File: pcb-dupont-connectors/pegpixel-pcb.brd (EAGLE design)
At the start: 21.6 x 14.2 mm, 5 parts

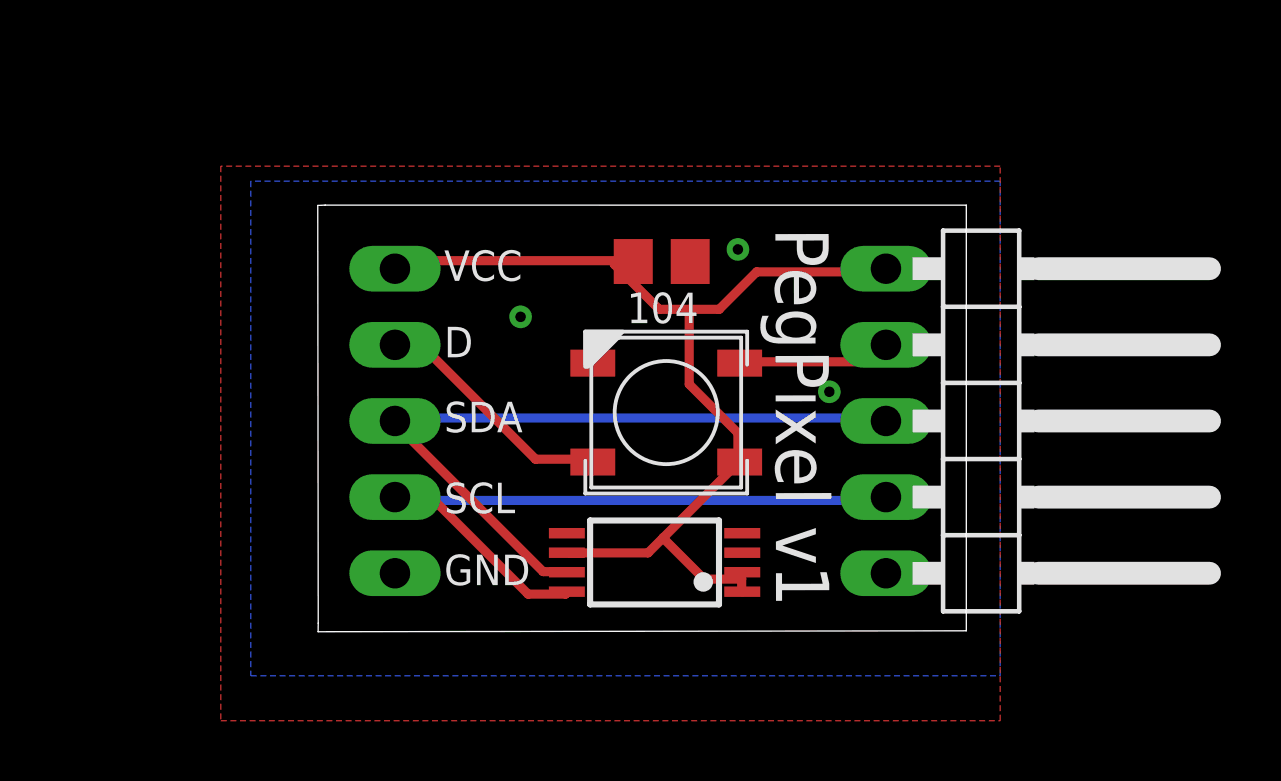
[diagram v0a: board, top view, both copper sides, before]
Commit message: mirror and turn input pin header to place it on top layer
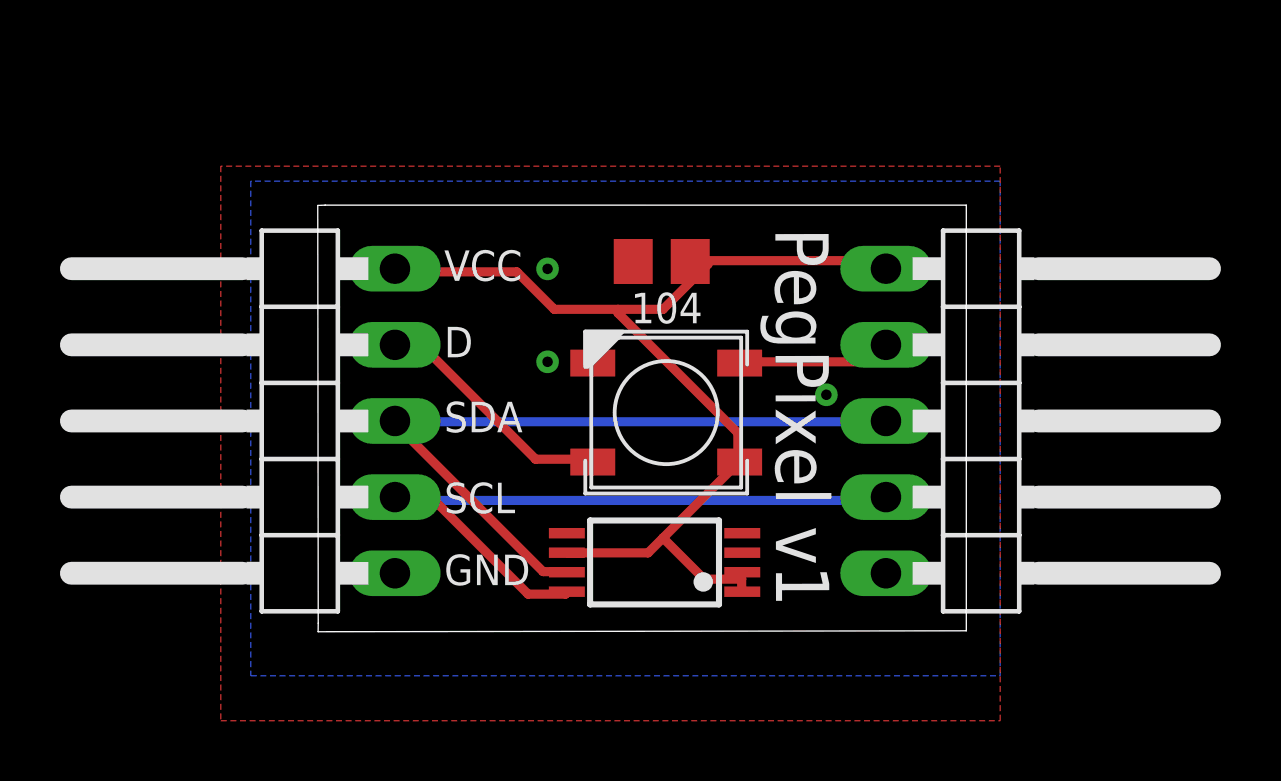
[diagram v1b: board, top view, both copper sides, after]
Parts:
- turned 104 to 180 degrees
- flipped JP1 to the top, turned to 90 degrees
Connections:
- net DIN: now also JP1.4; no longer JP1.2
- net GND: now also JP1.1; no longer JP1.5
- net SCL: now also JP1.2; no longer JP1.4
- net VCC: now also JP1.5; no longer JP1.1
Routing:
- net VCC: track 35.6 -> 36.5 mm
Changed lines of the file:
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@@
 </autorouter>
 <elements>
-<element name="104" library="rcl" library_urn="urn:adsk.eagle:library:334" package="C0805" package3d_urn="urn:adsk.eagle:package:23617/2" value="104" x="12.208859375" y="12.346228125" smashed="yes">
-<attribute name="SPICEPREFIX" value="C" x="42.688859375" y="8.536228125" size="1.778" layer="27" display="off"/>
-<attribute name="VALUE" x="13.438859375" y="11.306228125" size="1.016" layer="25" rot="R180"/>
+<element name="104" library="rcl" library_urn="urn:adsk.eagle:library:334" package="C0805" package3d_urn="urn:adsk.eagle:package:23617/2" value="104" x="12.208859375" y="12.346228125" smashed="yes" rot="R180">
+<attribute name="SPICEPREFIX" value="C" x="-18.271140625" y="16.156228125" size="1.778" layer="27" rot="R180" display="off"/>
+<attribute name="VALUE" x="11.178859375" y="10.286228125" size="1.016" layer="25"/>
 </element>
 <element name="H1" library="a1454" package="TSSOP8" package3d_urn="urn:adsk.eagle:package:20813/2" value="A1454SMD" x="11.968859375" y="2.306228125" smashed="yes" rot="R90"/>
@@
 <attribute name="VALUE" x="10.580859375" y="3.931228125" size="0.4064" layer="27" ratio="10"/>
 </element>
-<element name="JP1" library="pinhead" library_urn="urn:adsk.eagle:library:325" package="1X05/90" package3d_urn="urn:adsk.eagle:package:22467/2" value="" x="-0.501140625" y="7.026228125" smashed="yes" rot="MR270">
-<attribute name="VALUE" x="3.308859375" y="-1.228771875" size="1.27" layer="28" rot="MR0"/>
+<element name="JP1" library="pinhead" library_urn="urn:adsk.eagle:library:325" package="1X05/90" package3d_urn="urn:adsk.eagle:package:22467/2" value="" x="-0.501140625" y="7.026228125" smashed="yes" rot="R90">
+<attribute name="VALUE" x="3.308859375" y="15.281228125" size="1.27" layer="27" rot="R180"/>
 </element>
 <element name="JP2" library="pinhead" library_urn="urn:adsk.eagle:library:325" package="1X05/90" package3d_urn="urn:adsk.eagle:package:22467/2" value="" x="23.498859375" y="7.026228125" smashed="yes" rot="R270">
@@
 <contactref element="H1" pad="6"/>
 <contactref element="LED1" pad="1-VDD"/>
-<contactref element="JP1" pad="1"/>
 <contactref element="JP2" pad="1"/>
 <contactref element="104" pad="1"/>
+<contactref element="JP1" pad="5"/>
 <wire x1="14.875" y1="1.875" x2="14.875" y2="1.75" width="0.3048" layer="1"/>
 <wire x1="14.875" y1="1.75" x2="14.875" y2="1.375" width="0.3048" layer="1"/>
@@
 <wire x1="13.625" y1="1.75" x2="14.875" y2="1.75" width="0.3048" layer="1"/>
 <wire x1="12.25" y1="3.125" x2="13.625" y2="1.75" width="0.3048" layer="1"/>
-<wire x1="3.625" y1="12.375" x2="11.25" y2="12.375" width="0.3048" layer="1"/>
-<wire x1="3.375" y1="12.125" x2="3.625" y2="12.375" width="0.3048" layer="1"/>
-<wire x1="11.25" y1="12.375" x2="11.258859375" y2="12.346228125" width="0.3048" layer="1"/>
-<wire x1="3.375" y1="12.125" x2="3.308859375" y2="12.106228125" width="0.3048" layer="1"/>
-<wire x1="15.375" y1="12" x2="19.625" y2="12" width="0.3048" layer="1"/>
-<wire x1="14.125" y1="10.75" x2="15.375" y2="12" width="0.3048" layer="1"/>
-<wire x1="12.125" y1="10.75" x2="13.125" y2="10.75" width="0.3048" layer="1"/>
-<wire x1="13.125" y1="10.75" x2="14.125" y2="10.75" width="0.3048" layer="1"/>
-<wire x1="10.625" y1="12.25" x2="12.125" y2="10.75" width="0.3048" layer="1"/>
-<wire x1="19.625" y1="12" x2="19.688859375" y2="12.106228125" width="0.3048" layer="1"/>
-<wire x1="10.625" y1="12.25" x2="11.258859375" y2="12.346228125" width="0.3048" layer="1"/>
+<wire x1="19.375" y1="12.375" x2="13.25" y2="12.375" width="0.3048" layer="1"/>
+<wire x1="19.625" y1="12.125" x2="19.375" y2="12.375" width="0.3048" layer="1"/>
+<wire x1="13.25" y1="12.375" x2="13.158859375" y2="12.346228125" width="0.3048" layer="1"/>
+<wire x1="19.625" y1="12.125" x2="19.688859375" y2="12.106228125" width="0.3048" layer="1"/>
+<wire x1="7.375" y1="12" x2="3.375" y2="12" width="0.3048" layer="1"/>
+<wire x1="8.625" y1="10.75" x2="7.375" y2="12" width="0.3048" layer="1"/>
+<wire x1="12.25" y1="10.75" x2="10.75" y2="10.75" width="0.3048" layer="1"/>
+<wire x1="10.75" y1="10.75" x2="8.625" y2="10.75" width="0.3048" layer="1"/>
+<wire x1="13.75" y1="12.25" x2="12.25" y2="10.75" width="0.3048" layer="1"/>
+<wire x1="3.375" y1="12" x2="3.308859375" y2="12.106228125" width="0.3048" layer="1"/>
+<wire x1="13.75" y1="12.25" x2="13.158859375" y2="12.346228125" width="0.3048" layer="1"/>
 <wire x1="14.75" y1="6.625" x2="14.75" y2="5.75" width="0.3048" layer="1"/>
-<wire x1="13.125" y1="8.25" x2="14.75" y2="6.625" width="0.3048" layer="1"/>
-<wire x1="13.125" y1="10.75" x2="13.125" y2="8.25" width="0.3048" layer="1"/>
+<wire x1="10.75" y1="10.625" x2="14.75" y2="6.625" width="0.3048" layer="1"/>
 <wire x1="14.75" y1="5.75" x2="14.808859375" y2="5.656228125" width="0.3048" layer="1"/>
+<wire x1="10.75" y1="10.625" x2="10.75" y2="10.75" width="0.3048" layer="1"/>
 </signal>
 <signal name="SCL">
 <contactref element="H1" pad="8"/>
-<contactref element="JP1" pad="4"/>
 <contactref element="JP2" pad="4"/>
+<contactref element="JP1" pad="2"/>
 <wire x1="7.75" y1="1.25" x2="9" y2="1.25" width="0.3048" layer="1"/>
 <wire x1="4.625" y1="4.375" x2="7.75" y2="1.25" width="0.3048" layer="1"/>
@@
 <wire x1="9" y1="2" x2="9.043859375" y2="1.981228125" width="0.3048" layer="1"/>
 <wire x1="3.25" y1="7" x2="3.308859375" y2="7.026228125" width="0.3048" layer="1"/>
-<wire x1="3.375" y1="7.125" x2="19.625" y2="7.125" width="0.3048" layer="16"/>
-<wire x1="19.625" y1="7.125" x2="19.688859375" y2="7.026228125" width="0.3048" layer="16"/>
-<wire x1="3.375" y1="7.125" x2="3.308859375" y2="7.026228125" width="0.3048" layer="16"/>
+<wire x1="3.375" y1="7" x2="19.625" y2="7" width="0.3048" layer="16"/>
+<wire x1="19.625" y1="7" x2="19.688859375" y2="7.026228125" width="0.3048" layer="16"/>
+<wire x1="3.375" y1="7" x2="3.308859375" y2="7.026228125" width="0.3048" layer="16"/>
 </signal>
 <signal name="GND">
@@
 <vertex x="23.498859375" y="15.526228125"/>
 </polygon>
-<contactref element="JP1" pad="5"/>
 <contactref element="JP2" pad="5"/>
 <polygon width="0.1524" layer="16">
@@
 <vertex x="23.498859375" y="15.026228125"/>
 </polygon>
-<via x="7.5" y="10.5" extent="1-16" drill="0.35"/>
-<via x="14.75" y="12.75" extent="1-16" drill="0.35"/>
-<via x="17.8" y="8" extent="1-16" drill="0.35"/>
+<contactref element="JP1" pad="1"/>
+<via x="8.4" y="12.1" extent="1-16" drill="0.35"/>
+<via x="17.7" y="7.9" extent="1-16" drill="0.35"/>
+<via x="8.4" y="9" extent="1-16" drill="0.35"/>
 </signal>
 <signal name="DIN">
-<contactref element="JP1" pad="2"/>
 <contactref element="LED1" pad="4-DIN"/>
+<contactref element="JP1" pad="4"/>
 <wire x1="8" y1="5.75" x2="9.875" y2="5.75" width="0.3048" layer="1"/>
 <wire x1="4.25" y1="9.5" x2="8" y2="5.75" width="0.3048" layer="1"/>
